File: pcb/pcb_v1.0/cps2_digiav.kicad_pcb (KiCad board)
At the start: 2 copper layers, 93.6 x 46.2 mm, 134 parts, among them J4 HDMI_CONN, P1 JTAG_CONN, U10 S25FL116K, U12 TLV70012, U13 TLV70025, U14 TLV70012, U15 TLV70018, U16 TLV70018, U2 EP4CE15E22, U3 IT6613, U31 74LVC245, U32 74LVC245, U33 74LVC245, U34 SN74LVC3G17, U7 TC1262-3.3VDBTR, U8 TLV70033

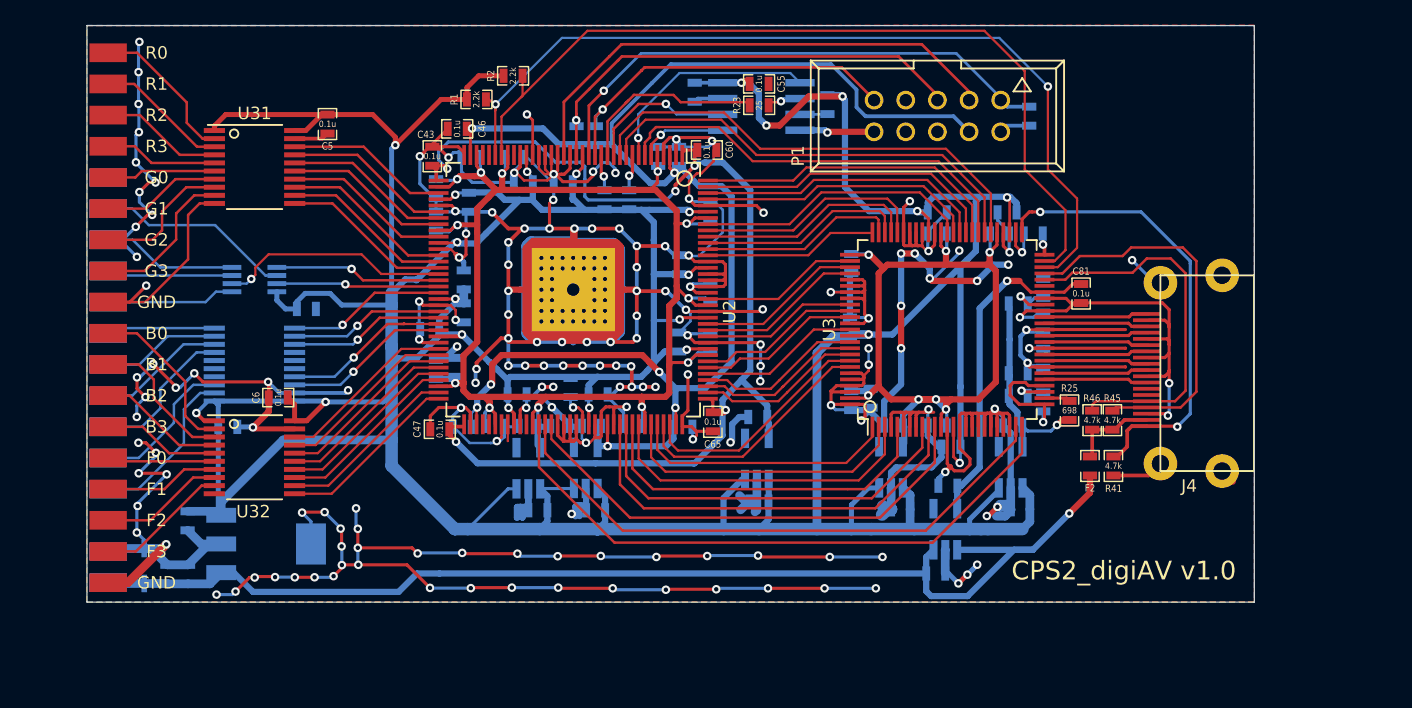
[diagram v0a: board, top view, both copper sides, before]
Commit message: This is a combination of 10 commits.
Moved ICs to top, made to fit ontop of CPS2 DIPs

Added ADV7513

update lib path

Finished power section of ADV7531

initial layout of ADV7513

Added Si5351C

Reordered inputs, improved clock layout

Final changes before pull req

Removing auto-generated files

Removing remaining auto-generated files
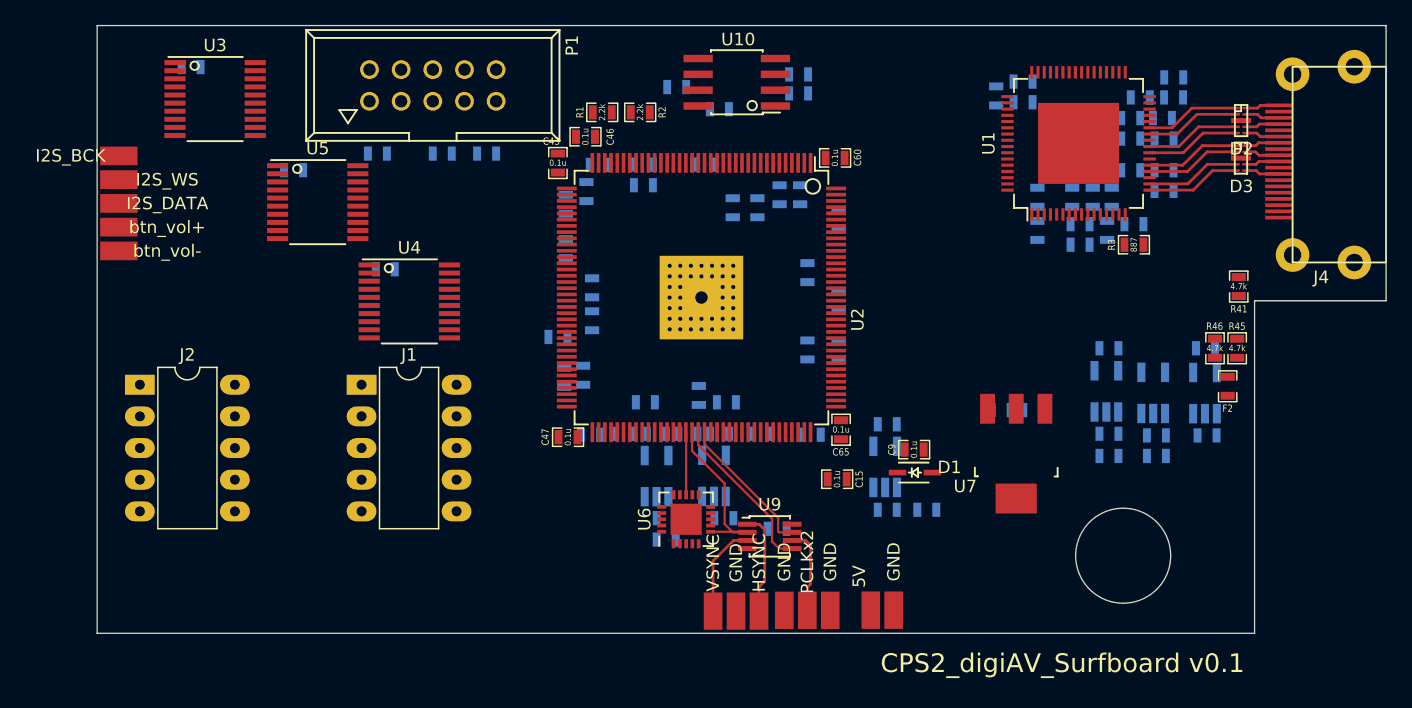
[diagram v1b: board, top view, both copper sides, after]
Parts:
- removed R25: 698, custom_components:SM0603_Resistor_libcms
- removed R26: 1k, custom_components:SM0603_Resistor_libcms
- removed U31, U32, U33: 74LVC245, custom_components:TSSOP-20_4.4x6.5mm_Pitch0.65mm_Handsoldering
- removed U34: SN74LVC3G17, custom_components:SSOP-8_3x3mm_Pitch0.65mm
- removed W14: B3, custom_components:SMD_PAD
- removed W15: F0, custom_components:SMD_PAD
- removed W16: F1, custom_components:SMD_PAD
- removed W17: F2, custom_components:SMD_PAD
- removed W18: F3, custom_components:SMD_PAD
- removed W19: btn_vol+, custom_components:SMD_PAD
- removed W20: I2S_BCK, custom_components:SMD_PAD
- removed W21: PCLKx2, custom_components:SMD_PAD
- removed W22: I2S_WS, custom_components:SMD_PAD
- removed W23: btn_vol-, custom_components:SMD_PAD
- removed W24: VSYNC, custom_components:SMD_PAD
- removed W25: I2S_DATA, custom_components:SMD_PAD
- removed W26: HSYNC, custom_components:SMD_PAD
- removed W27, W28, W29, W30, W31: GND, custom_components:SMD_PAD
- added C10: 10u, custom_components:SM0603_Capa_libcms, B.Cu at (114.5, 40.0)
- added C11: 10u, custom_components:SM0603_Capa_libcms, B.Cu at (124.6, 30.9)
- added C12: 10u, custom_components:SM0603_Capa_libcms, B.Cu at (117.3, 37.3)
- added C13: 10u, custom_components:SM0603_Capa_libcms, B.Cu at (124.7, 32.6)
- added C14: 0.1u, custom_components:SM0603_Capa_libcms, B.Cu at (93.7, 63.9)
- added C15: 0.1u, custom_components:SM0603_Capa_libcms, F.Cu at (98.5, 59.9)
- added D2: RClamp0524P, Custom_OSSC:SLP2510P8, F.Cu at (130.9, 31.1)
- added D3: RClamp0524P, Custom_OSSC:SLP2510P8, F.Cu at (130.9, 34.2)
- added FB3: MPZ1608S221A, custom_components:SM0603_Resistor_libcms, B.Cu at (113.4, 29.7)
- added J1: Conn_02x05, Housings_DIP:DIP-10_W7.62mm_LongPads, F.Cu at (60.3, 52.3)
- added J2: Conn_02x05, Housings_DIP:DIP-10_W7.62mm_LongPads, F.Cu at (42.5, 52.3)
- added R3: 887, custom_components:SM0603_Resistor_libcms, F.Cu at (122.3, 41.1)
- added R4: 4.7k, custom_components:SM0603_Resistor_libcms, B.Cu at (84.8, 64.7)
- added U1: ADV7513, Housings_QFP:LQFP-64-1EP_10x10mm_Pitch0.5mm, F.Cu at (117.8, 33.0)
- added U4: 74LVC245, custom_components:TSSOP-20_4.4x6.5mm_Pitch0.65mm_Handsoldering, F.Cu at (64.2, 45.6)
- added U5: 74LVC245, custom_components:TSSOP-20_4.4x6.5mm_Pitch0.65mm_Handsoldering, F.Cu at (56.8, 37.7)
- added U6: SI5351C-B, Housings_DFN_QFN:QFN-20-1EP_4x4mm_Pitch0.5mm, F.Cu at (86.4, 63.1)
- added U9: SN74LVC3G17, custom_components:SSOP-8_3x3mm_Pitch0.65mm, F.Cu at (93.1, 64.5)
- C5: value 0.1u -> 47u; moved to B.Cu
- C55, C6, C81, R23: moved to B.Cu
- C9: value 47u -> 0.1u; moved to F.Cu
- D1, U10, U7, W1: moved to F.Cu
- U3: value IT6613 -> 74LVC245; footprint custom_components:TQFP-100_custom -> custom_components:TSSOP-20_4.4x6.5mm_Pitch0.65mm_Handsoldering
- W10: value G3 -> GND
- W11: value B0 -> HSYNC
- W12: value B1 -> VSYNC
- W13: value B2 -> PCLKx2
- W2: value GND -> I2S_BCK; moved to F.Cu
- W3: value R0 -> I2S_WS
- W4: value R1 -> I2S_DATA
- W5: value R2 -> btn_vol+
- W6: value R3 -> btn_vol-
- W7: value G0 -> GND
- W8: value G1 -> GND
- W9: value G2 -> GND
- moved W9 69.7 mm to (103.0, 70.4), turned to 90 degrees
- moved C1 69.0 mm to (114.2, 54.4), turned to 180 degrees
- moved W8 66.3 mm to (97.9, 70.4), turned to 90 degrees
- moved C3 65.9 mm to (111.6, 54.4), turned to 0 degrees
- moved D1 62.3 mm to (104.7, 59.4), turned to 0 degrees
- moved U3 61.6 mm to (48.6, 29.4), turned to 0 degrees
- moved W1 61.2 mm to (101.2, 70.4), turned to 90 degrees
- moved W7 61.2 mm to (90.4, 70.5), turned to 90 degrees
- moved C9 60.7 mm to (104.6, 57.5), turned to 0 degrees
- moved W10 60.7 mm to (94.2, 70.4), turned to 90 degrees
- moved U7 60.6 mm to (112.8, 57.9), turned to 180 degrees
- moved W13 58.7 mm to (96.1, 70.4), turned to 90 degrees
- moved C5 57.2 mm to (105.7, 62.4), turned to 0 degrees
- moved W11 56.8 mm to (92.2, 70.5), turned to 90 degrees
- moved W12 52.4 mm to (88.5, 70.5), turned to 90 degrees
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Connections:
- C101 pad 1: /IOVDD -> /hdmitx1/DVDD3V3
- C108 pad 1: /IOVDD -> /hdmitx1/DVDD3V3
- C110 pad 1: /hdmitx1/DVDD1V8 -> /hdmitx1/AVDD1V8
- C3 pad 1: /IOVDD -> /hdmitx1/DVDD3V3
- C4 pad 1: /A33VDD -> /hdmitx1/AVDD3V3
- C40 pad 1: /IOVDD -> /hdmitx1/DVDD3V3
- C45 pad 1: /IOVDD -> /hdmitx1/DVDD3V3
- C5 pad 1: GND -> /input1/5V
- C5 pad 2: /IOVDD -> GND
- C52 pad 1: /IOVDD -> /hdmitx1/DVDD3V3
- C53 pad 1: /IOVDD -> /hdmitx1/DVDD3V3
- C55 pad 2: /IOVDD -> /hdmitx1/DVDD3V3
- C57 pad 1: /IOVDD -> /hdmitx1/DVDD3V3
- C6 pad 2: /IOVDD -> /hdmitx1/DVDD3V3
- C62 pad 1: /IOVDD -> /hdmitx1/DVDD3V3
- C63 pad 1: /IOVDD -> /hdmitx1/DVDD3V3
- C69 pad 1: /hdmitx1/DVDD1V8 -> Net-(C12-Pad1)
- C7 pad 2: /IOVDD -> /hdmitx1/DVDD3V3
- C73 pad 1: /IOVDD -> Net-(C12-Pad1)
- C74 pad 1: Net-(C74-Pad1) -> /hdmitx1/DVDD1V8
- C75 pad 1: /hdmitx1/DVDD1V8 -> /hdmitx1/DVDD3V3
- C77 pad 1: Net-(C77-Pad1) -> Net-(C10-Pad1)
- C78 pad 1: Net-(C77-Pad1) -> Net-(C10-Pad1)
- C79 pad 1: /IOVDD -> Net-(C13-Pad1)
- C8 pad 1: /IOVDD -> GND
- C8 pad 2: GND -> /hdmitx1/DVDD3V3
- C80 pad 1: Net-(C80-Pad1) -> Net-(C10-Pad1)
- C81 pad 1: /A33VDD -> Net-(C10-Pad1)
- C82 pad 1: /hdmitx1/DVDD1V8 -> Net-(C11-Pad1)
- C83 pad 1: /IOVDD -> Net-(C13-Pad1)
- C84 pad 1: /hdmitx1/DVDD1V8 -> Net-(C13-Pad1)
- C85 pad 1: /hdmitx1/DVDD1V8 -> /hdmitx1/AVDD1V8
- C86 pad 1: /IOVDD -> /hdmitx1/AVDD1V8
- C87 pad 1: /IOVDD -> /hdmitx1/DVDD3V3
- C88 pad 1: /IOVDD -> /hdmitx1/AVDD3V3
- C9 pad 1: /5V -> GND
- C9 pad 2: GND -> /hdmitx1/DVDD3V3
- C90 pad 1: /hdmitx1/AVCC1V8 -> /hdmitx1/AVDD1V8
- C91 pad 1: /IOVDD -> /hdmitx1/DVDD3V3
- C92 pad 1: /IOVDD -> /hdmitx1/DVDD3V3
- C94 pad 1: /IOVDD -> /hdmitx1/DVDD3V3
- C99 pad 1: /IOVDD -> /hdmitx1/DVDD3V3
- D1 pad 1: /5V -> /input1/5V
- FB1 pad 1: /hdmitx1/AVCC1V8 -> Net-(C13-Pad1)
- FB1 pad 2: Net-(C74-Pad1) -> /hdmitx1/AVDD1V8
- FB2 pad 1: /hdmitx1/AVCC1V8 -> Net-(C12-Pad1)
- FB2 pad 2: Net-(C77-Pad1) -> /hdmitx1/AVDD1V8
- FB4 pad 1: /hdmitx1/AVCC1V8 -> /hdmitx1/DVDD3V3
- FB4 pad 2: Net-(C80-Pad1) -> Net-(C11-Pad1)
- J4 pad 1: /hdmitx1/TMDS_D2+ -> Net-(D2-Pad10)
- J4 pad 10: /hdmitx1/TMDS_CLK+ -> Net-(D3-Pad7)
- J4 pad 12: /hdmitx1/TMDS_CLK- -> Net-(D3-Pad6)
- J4 pad 13: Net-(J4-Pad13) -> (no net)
- J4 pad 14: Net-(J4-Pad14) -> (no net)
- J4 pad 15: /hdmitx1/DDC_SCL -> /hdmitx1/DDCSCL
- J4 pad 16: /hdmitx1/DDC_SDA -> /hdmitx1/DDCSDA
- J4 pad 3: /hdmitx1/TMDS_D2- -> Net-(D2-Pad9)
- J4 pad 4: /hdmitx1/TMDS_D1+ -> Net-(D2-Pad7)
- J4 pad 6: /hdmitx1/TMDS_D1- -> Net-(D2-Pad6)
- J4 pad 7: /hdmitx1/TMDS_D0+ -> Net-(D3-Pad10)
- J4 pad 9: /hdmitx1/TMDS_D0- -> Net-(D3-Pad9)
- P1 pad 6: Net-(P1-Pad6) -> (no net)
- P1 pad 7: Net-(P1-Pad7) -> (no net)
- P1 pad 8: Net-(P1-Pad8) -> (no net)
- R1 pad 1: /IOVDD -> /hdmitx1/DVDD3V3
- R16 pad 1: /IOVDD -> /hdmitx1/DVDD3V3
- R17 pad 2: /IOVDD -> /hdmitx1/DVDD3V3
- R18 pad 1: /IOVDD -> /hdmitx1/DVDD3V3
- R19 pad 2: /IOVDD -> /hdmitx1/DVDD3V3
- R2 pad 1: /IOVDD -> /hdmitx1/DVDD3V3
- R24 pad 2: /IOVDD -> /hdmitx1/DVDD3V3
- R45 pad 2: /hdmitx1/DDC_SDA -> /hdmitx1/DDCSDA
- R46 pad 2: /hdmitx1/DDC_SCL -> /hdmitx1/DDCSCL
- U10 pad 8: /IOVDD -> /hdmitx1/DVDD3V3
- U12 pad 1: /IOVDD -> /hdmitx1/DVDD3V3
- U12 pad 3: /IOVDD -> /hdmitx1/DVDD3V3
- U13 pad 1: /IOVDD -> /hdmitx1/DVDD3V3
- U13 pad 3: /IOVDD -> /hdmitx1/DVDD3V3
- U14 pad 1: /IOVDD -> /hdmitx1/DVDD3V3
- U14 pad 3: /IOVDD -> /hdmitx1/DVDD3V3
- U15 pad 1: /IOVDD -> /hdmitx1/DVDD3V3
- U15 pad 3: /IOVDD -> /hdmitx1/DVDD3V3
- U16 pad 1: /IOVDD -> /hdmitx1/AVDD3V3
- U16 pad 3: /IOVDD -> /hdmitx1/AVDD3V3
- U16 pad 5: /hdmitx1/AVCC1V8 -> /hdmitx1/AVDD1V8
- U2 pad 113: /fpga1/HDMITX_PCLK -> /hdmitx1/B5
- U2 pad 114: /hdmitx1/B5 -> /hdmitx1/B6
- U2 pad 115: /hdmitx1/B6 -> /hdmitx1/B7
- U2 pad 117: /IOVDD -> /hdmitx1/DVDD3V3
- U2 pad 119: /hdmitx1/B7 -> /hdmitx1/G0
- U2 pad 120: /hdmitx1/G0 -> /fpga1/HDMITX_PCLK
- U2 pad 122: /IOVDD -> /hdmitx1/DVDD3V3
- U2 pad 130: /IOVDD -> /hdmitx1/DVDD3V3
- U2 pad 139: /IOVDD -> /hdmitx1/DVDD3V3
- U2 pad 17: /IOVDD -> /hdmitx1/DVDD3V3
- U2 pad 26: /IOVDD -> /hdmitx1/DVDD3V3
- U2 pad 28: Net-(U2-Pad28) -> (no net)
- U2 pad 32: Net-(U2-Pad32) -> (no net)
- U2 pad 33: Net-(U2-Pad33) -> (no net)
- U2 pad 39: /fpga1/Rin0 -> /input1/F3_O
- U2 pad 40: /IOVDD -> /hdmitx1/DVDD3V3
- U2 pad 42: /fpga1/Rin1 -> /input1/F2_O
- U2 pad 43: /fpga1/Rin2 -> /input1/F1_O
- U2 pad 44: /fpga1/Rin3 -> /input1/F0_O
- U2 pad 46: /fpga1/Gin0 -> /input1/R3_O
- U2 pad 47: /IOVDD -> /hdmitx1/DVDD3V3
- U2 pad 49: /fpga1/Gin1 -> /input1/R2_O
- U2 pad 50: /fpga1/Gin2 -> /input1/R1_O
- U2 pad 51: /fpga1/Gin3 -> /input1/R0_O
- U2 pad 52: /fpga1/PCLKx2_in -> GND
- U2 pad 53: /fpga1/VSYNC_in -> GND
- U2 pad 54: /fpga1/HSYNC_in -> GND
- U2 pad 56: /IOVDD -> /hdmitx1/DVDD3V3
- U2 pad 60: /fpga1/btn_vol+ -> /input1/VOL+_O
- U2 pad 61: /fpga1/btn_vol- -> /input1/VOL-_O
- U2 pad 62: /IOVDD -> /hdmitx1/DVDD3V3
- U2 pad 64: /fpga1/Bin0 -> /input1/G3_O
- U2 pad 65: /fpga1/Bin1 -> /input1/G2_O
- U2 pad 66: /fpga1/Bin2 -> /input1/G1_O
- U2 pad 67: /fpga1/Bin3 -> /input1/G0_O
- U2 pad 68: /fpga1/Fin0 -> /input1/B3_O
- U2 pad 69: /fpga1/Fin1 -> /input1/B2_O
- U2 pad 71: /fpga1/Fin2 -> /input1/B1_O
- U2 pad 72: /fpga1/Fin3 -> /input1/B0_O
- U2 pad 76: Net-(U2-Pad76) -> (no net)
- U2 pad 77: Net-(U2-Pad77) -> (no net)
- U2 pad 80: Net-(U2-Pad80) -> (no net)
- U2 pad 81: /IOVDD -> /hdmitx1/DVDD3V3
- U2 pad 83: Net-(U2-Pad83) -> (no net)
- U2 pad 88: GND -> /fpga1/CLK0
- U2 pad 89: GND -> /input1/PCLKx2
- U2 pad 90: GND -> /input1/VSYNC_O
- U2 pad 91: GND -> /input1/HSYNC_O
- U2 pad 93: /IOVDD -> /hdmitx1/DVDD3V3
- U3 pad 1: /hdmitx1/DE -> /hdmitx1/DVDD3V3
- U3 pad 10: /fpga1/HDMITX_I2S_WS -> GND
- U3 pad 11: /fpga1/HDMITX_I2S_BCK -> /input1/R0_O
- U3 pad 12: /hdmitx1/DVDD1V8 -> /input1/R1_O
- U3 pad 13: GND -> /input1/R2_O
- U3 pad 14: /IOVDD -> /input1/R3_O
- U3 pad 15: GND -> /input1/F0_O
- U3 pad 16: GND -> /input1/F1_O
- U3 pad 17: GND -> /input1/F2_O
- U3 pad 18: GND -> /input1/F3_O
- U3 pad 2: /fpga1/HDMITX_HSYNC -> Net-(J2-Pad10)
- U3 pad 20: GND -> /hdmitx1/DVDD3V3
- U3 pad 3: /fpga1/HDMITX_VSYNC -> Net-(J2-Pad9)
- U3 pad 4: GND -> Net-(J2-Pad8)
- U3 pad 5: /fpga1/AUD_MCLK -> Net-(J2-Pad7)
- U3 pad 6: GND -> Net-(J2-Pad6)
- U3 pad 7: GND -> Net-(J2-Pad4)
- U3 pad 8: GND -> Net-(J2-Pad3)
- U3 pad 9: /fpga1/HDMITX_I2S_DATA -> Net-(J2-Pad2)
- U7 pad 3: /IOVDD -> /hdmitx1/DVDD3V3
- U8 pad 5: /A33VDD -> /hdmitx1/AVDD3V3
- W1 pad 1: /5V -> /input1/5V
- W10 pad 1: Net-(U31-Pad9) -> GND
- W2 pad 1: GND -> Net-(U5-Pad2)
- W7 pad 1: Net-(U31-Pad6) -> GND
- W8 pad 1: Net-(U31-Pad7) -> GND
- W9 pad 1: Net-(U31-Pad8) -> GND
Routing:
- net GND: track 885.6 -> 0.00 mm, vias 171 -> 0
- net /IOVDD: track 450.2 -> 0.00 mm, vias 22 -> 0
- net /fpga1/VCCINT: track 131.2 -> 0.00 mm, vias 12 -> 0
- net /fpga1/VCCA: track 125.2 -> 0.00 mm, vias 7 -> 0
- net /5V: track 95.5 -> 0.00 mm, vias 1 -> 0
- net /fpga1/VCCD_PLL: track 93.4 -> 0.00 mm, vias 5 -> 0
- net /fpga1/SCL: track 70.7 -> 0.00 mm, vias 2 -> 0
- net /fpga1/SDA: track 68.7 -> 0.00 mm
- net /hdmitx1/DVDD1V8: track 65.9 -> 0.00 mm, vias 7 -> 0
- net /fpga1/HDMITX_RESET_N: track 49.8 -> 0.00 mm
- net /fpga1/HDMITX_INT_N: track 46.7 -> 0.00 mm
- net /fpga1/TCK: track 42.7 -> 0.00 mm, vias 1 -> 0
- net /fpga1/TDO: track 40.7 -> 0.00 mm
- net /fpga1/HDMITX_I2S_BCK: track 39.1 -> 0.00 mm
- net /fpga1/HDMITX_R7: track 37.8 -> 0.00 mm
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- removed copper zone on B.Cu, net GND
- removed copper zone on F.Cu, net GND
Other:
- board size 93.6 x 46.2 mm -> 103.4 x 48.7 mm
- board text added: "CPS2_digiAV_Surfboard v0.1"
- board text removed: "CPS2_digiAV v1.0"
